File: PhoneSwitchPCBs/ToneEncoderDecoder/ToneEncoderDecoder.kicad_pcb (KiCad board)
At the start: 2 copper layers, 100 x 100 mm, 124 parts, among them IC1 XRA1203IG24TR-F, IC2 NXB0108PWJ, IC3 74HC4316, IC4 74HC4316, IC5 TL074*DT, IC6 TL074*DT, IC7 TL072, IC8 MT8870DN1, IC9 MT8870DN1, J1 Tone Bus, J2 Power + Control, Q1 XP231N02013R-G, Q2 XP231N02013R-G, Y1 3.579545 MHz

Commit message: Finish routing (for the first time)
Okay, unrouted nets says 0.  However, this could probably use some cleanup.
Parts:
- C1, C2, Q1, Q2, R49, R50, R51, R52: moved to B.Cu
- D7, D8: moved to F.Cu
- moved C17 181.0 mm to (72.2, 63.1), turned to 90 degrees
- moved C1 174.3 mm to (52.8, 67.4)
- moved R49 173.4 mm to (60.3, 62.6)
- moved R52 155.8 mm to (94.5, 70.5), turned to 90 degrees
- moved Q1 150.2 mm to (58.2, 66.0), turned to -90 degrees
- moved R51 148.3 mm to (96.8, 65.9), turned to 90 degrees
- moved R50 143.0 mm to (58.2, 70.4), turned to 90 degrees
- moved C2 138.4 mm to (88.8, 65.4)
- moved C40 114.2 mm to (105.2, 28.2), turned to -90 degrees
- moved C42 113.9 mm to (105.2, 32.4), turned to 90 degrees
- moved C39 107.3 mm to (108.0, 28.2), turned to 90 degrees
- moved C41 93.8 mm to (108.0, 32.4), turned to 90 degrees
- moved D8 60.6 mm to (100.8, 67.0), turned to 0 degrees
- moved D7 54.3 mm to (100.8, 58.5), turned to 0 degrees
- moved Q2 38.7 mm to (94.5, 66.0), turned to -90 degrees
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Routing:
- net +5VD: track 37.2 -> 137.7 mm, vias 2 -> 6
- net +3V3: track 22.1 -> 118.6 mm, vias 3 -> 6
- net +5VA: track 109.4 -> 198.7 mm
- net -5VA: track 103.6 -> 173.0 mm, vias 7 -> 11
- net /A1: track 0.00 -> 69.2 mm, vias 0 -> 1
- net /TI1: track 0.00 -> 65.0 mm, vias 0 -> 1
- net /T2: track 8.10 -> 63.0 mm, vias 0 -> 3
- net /SCL: track 0.00 -> 54.3 mm, vias 0 -> 1
- net /A0: track 0.00 -> 52.7 mm, vias 0 -> 2
- net /SDA: track 0.00 -> 50.1 mm, vias 0 -> 1
- net /TI2: track 0.00 -> 42.8 mm, vias 0 -> 1
- net /T1: track 86.5 -> 107.8 mm, vias 1 -> 3
- net /DH1: track 0.00 -> 7.71 mm, vias 0 -> 1
- net /DH2: track 0.00 -> 7.55 mm, vias 0 -> 1
- net Net-(C34-Pad1): track 24.2 -> 27.5 mm
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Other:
- board size 100 x 100 mm -> 100 x 70 mm

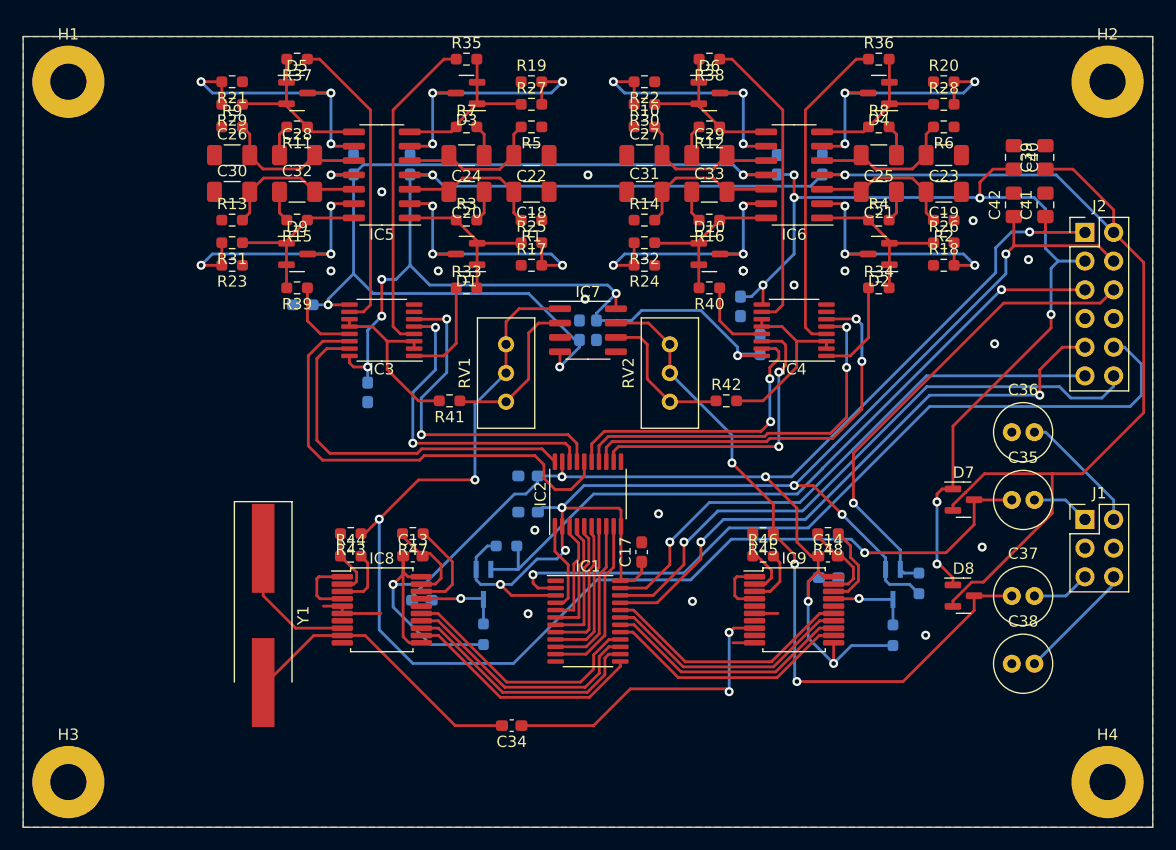
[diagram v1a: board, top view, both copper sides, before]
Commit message: Arrange Silkscreen Values
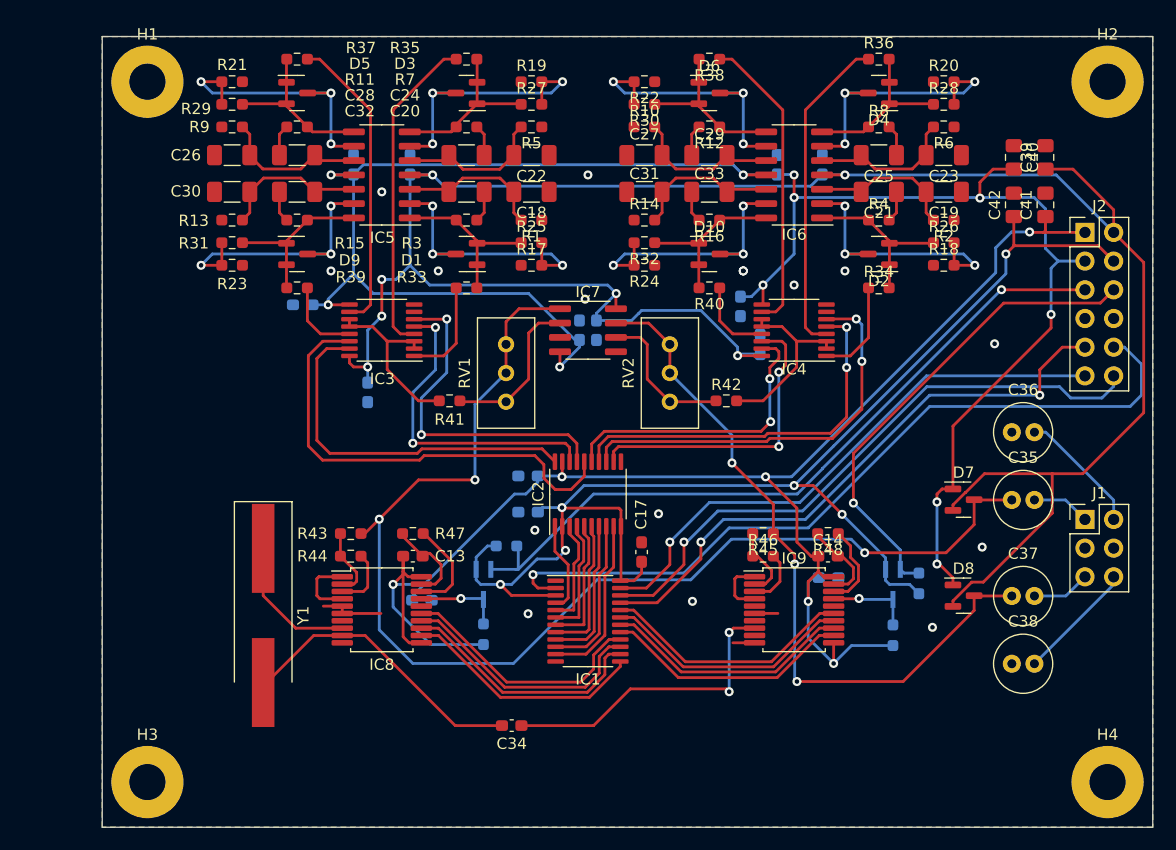
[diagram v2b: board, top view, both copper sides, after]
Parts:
- moved H1 7.00 mm to (28.5, 21.5)
- moved H3 7.00 mm to (28.5, 83.5)
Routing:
- net GND: vias 18 -> 16
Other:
- board size 100 x 70 mm -> 93 x 70 mm

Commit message: Finishing touches on PCB design
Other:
- board text added: "TeleTech MiniSwitch DTMF Decoder and Call Progress Tone Generator"
